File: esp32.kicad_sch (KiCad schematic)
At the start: 20 parts, among them SW4 PTS526_SM08_SMTR2_LFS

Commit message: more routing
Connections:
- net RFM95W_DI0: now reaches IC?.18 (IO14)
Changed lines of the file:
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@@
+    )
+  )
+  (global_label "RFM95W_DI0" (shape input) (at 111.76 54.61 180) (fields_autoplaced)
+    (effects (font (size 1.27 1.27)) (justify right))
+    (property "Intersheetrefs" "${INTERSHEET_REFS}" (at 97.0425 54.61 0)
+      (effects (font (size 1.27 1.27)) (justify right) hide)
     )
   )

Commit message: more routing
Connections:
- net VBUS: now also J?.A4 (VBUS), J?.A9 (VBUS), J?.B4 (VBUS), J?.B9 (VBUS)
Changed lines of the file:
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@@
+    )
+  )
+  (global_label "VBUS" (shape input) (at 265.43 118.11 0) (fields_autoplaced)
+    (effects (font (size 1.27 1.27)) (justify left))
+    (property "Intersheetrefs" "${INTERSHEET_REFS}" (at 273.3138 118.11 0)
+      (effects (font (size 1.27 1.27)) (justify left) hide)
     )
   )

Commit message: significant amount of routing done
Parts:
- removed SW4: PTS526_SM08_SMTR2_LFS, PTS526_SM08_SMTR2_LFS:SW_PTS526_SM08_SMTR2_LFS, symbol PTS526_SM08_SMTR2_LFS:PTS526_SM08_SMTR2_LFS
- removed SW?: TDD01H0SB1R, TDD01H0SB1R:SOT175P420X230-3N, symbol TDD01H0SB1R:TDD01H0SB1R
- added D? (x8): LED, LED_SMD:LED_0402_1005Metric, symbol Device:LED
- added R? (x8): 2.2k, Resistor_SMD:R_0402_1005Metric, symbol Device:R
- added S1: CJS-1200TA, CJS-1200TA:SW_CJS-1200TA, symbol CJS-1200TA:CJS-1200TA
- added S3: B3U-1000P, B3U-1000P:SW_B3U-1000P, symbol B3U-1000P:B3U-1000P
- D?: value WS2812B -> WS2812B-2020; footprint LED_SMD:LED_WS2812B_PLCC4_5.0x5.0mm_P3.2mm -> LED_SMD:LED_WS2812B-2020_PLCC4_2.0x2.0mm
- R? (x3): footprint Resistor_SMD:R_0603_1608Metric -> Resistor_SMD:R_0402_1005Metric
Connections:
- net ESP32-EN: now also S3.2
- net ESP32-GPIO0: now also S1.3
- net ESP32-RX0: no longer IC?.40 (RXD0)
- net ESP32-TX0: no longer IC?.39 (TXD0)
- net GND: now also D?.1 (K), D?.1 (K), D?.1 (K), D?.1 (K), D?.1 (K), D?.1 (K), D?.1 (K), D?.1 (K), S1.2, S3.1
- net RFM95W_RST: now reaches IC?.13 (IO9)
- net CROSS_UART: now reaches IC?.34 (IO38)
- net CROSS_UART: now also R?.2
- net CROSS_I2C: now reaches IC?.35 (IO39)
- net CROSS_I2C: now also R?.2
- net CROSS_SPI: now reaches IC?.36 (IO40)
- net CROSS_SPI: now also R?.2
- net RFD_900: now reaches IC?.37 (IO41)
- net RFD_900: now also R?.2
- net SPI-1_ESP32: now reaches IC?.38 (IO42)
- net SPI-1_ESP32: now also R?.2
- net I2C-1_STM32: now reaches IC?.41 (IO45)
- net I2C-1_STM32: now also R?.2
- net BUZZ_IN: now reaches IC?.5 (IO1)
- new net: D?.2 (A), R?.1 (x8)
- new net SPI-1_STM32: IC?.39 (TXD0), R?.2
- new net SPI-2_STM32: IC?.40 (RXD0), R?.2
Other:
- moved on the sheet: C?, R17

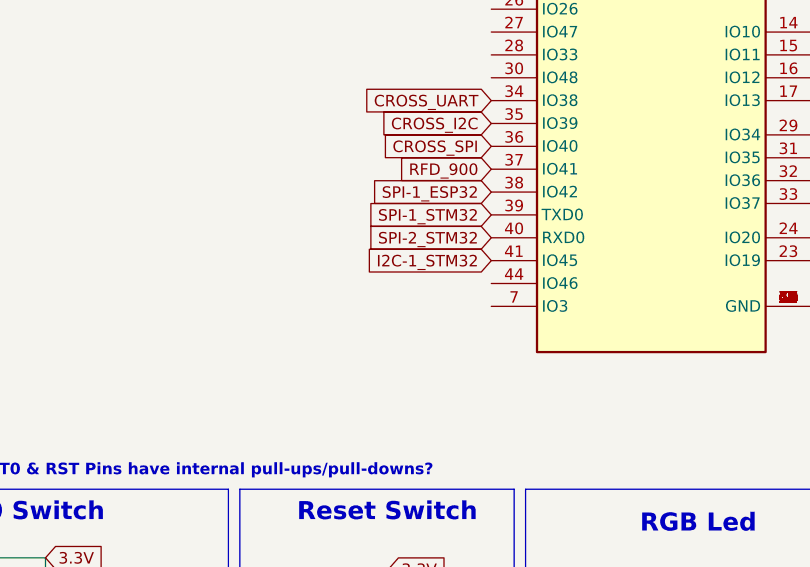
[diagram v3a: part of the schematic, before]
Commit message: signals routed
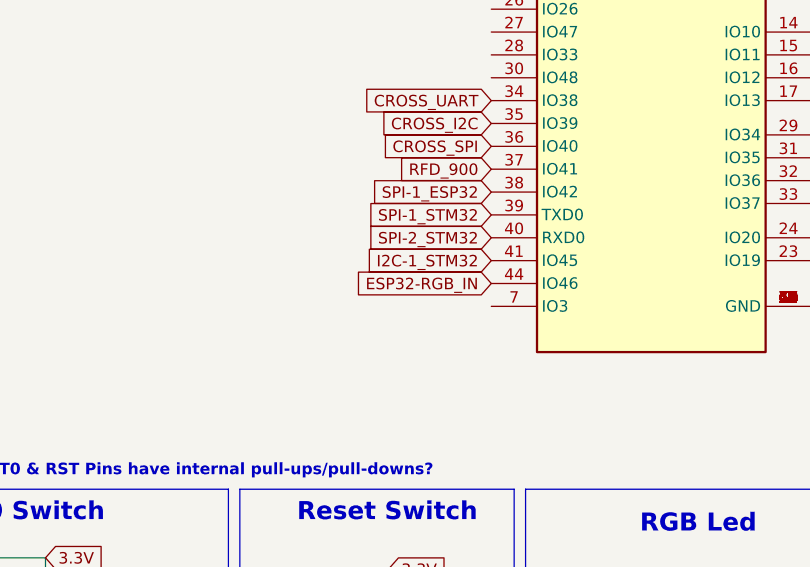
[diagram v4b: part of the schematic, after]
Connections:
- net ESP32-RGB_IN: now also IC?.44 (IO46)
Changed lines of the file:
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@@
+    )
+  )
+  (global_label "ESP32-RGB_IN" (shape input) (at 111.76 90.17 180) (fields_autoplaced)
+    (effects (font (size 1.27 1.27)) (justify right))
+    (property "Intersheetrefs" "${INTERSHEET_REFS}" (at 94.442 90.17 0)
+      (effects (font (size 1.27 1.27)) (justify right) hide)
     )
   )

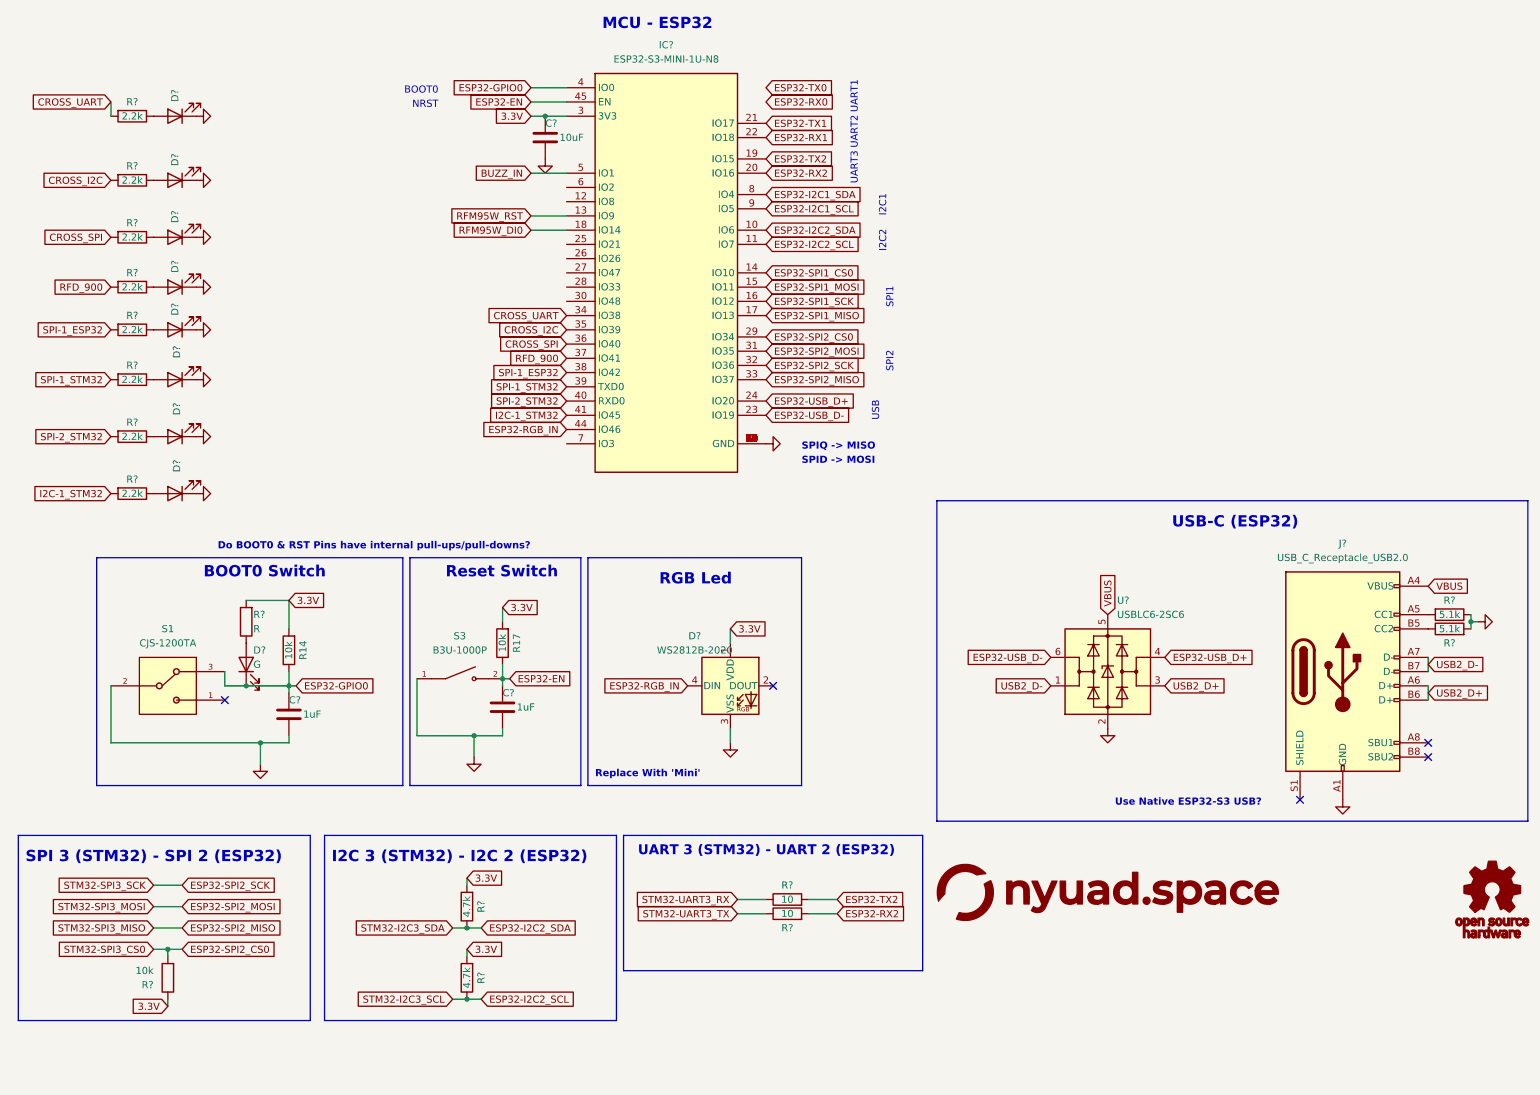
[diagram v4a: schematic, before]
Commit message: updated schematics
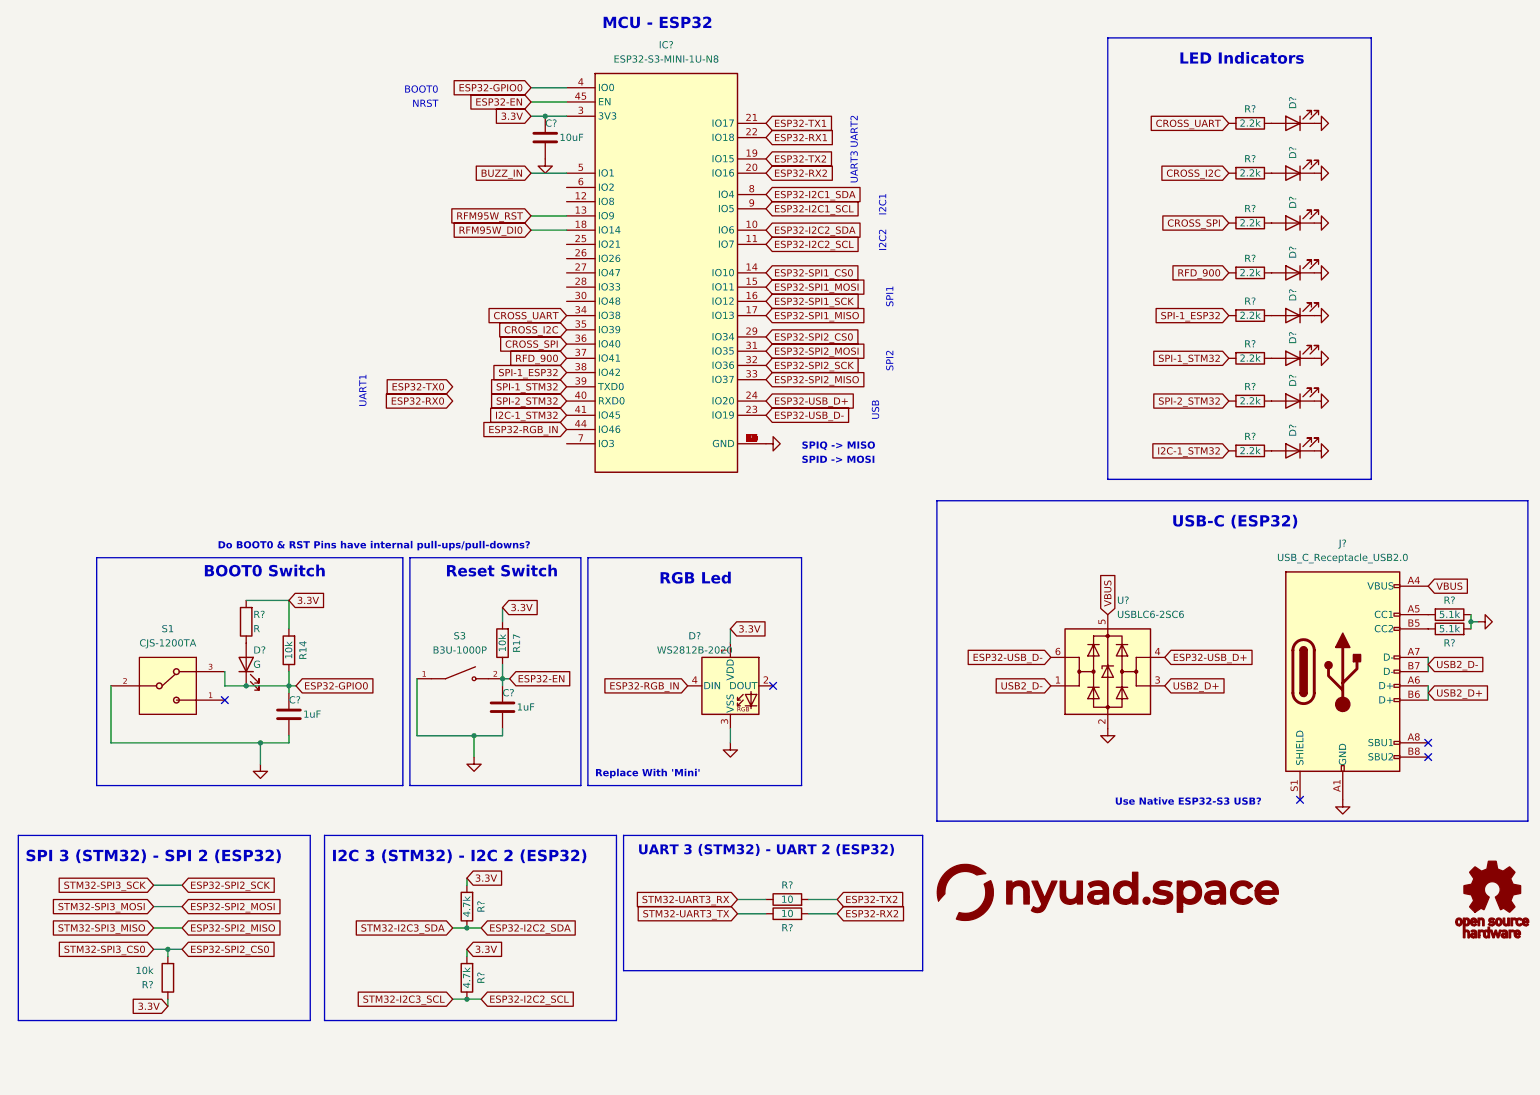
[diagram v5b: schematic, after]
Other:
- note added: "LED Indicators"
- moved on the sheet: D?, R?

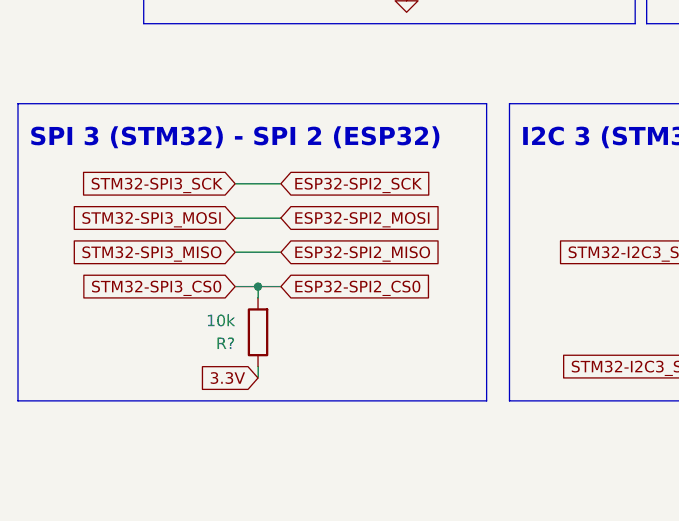
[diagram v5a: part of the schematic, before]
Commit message: added power planes
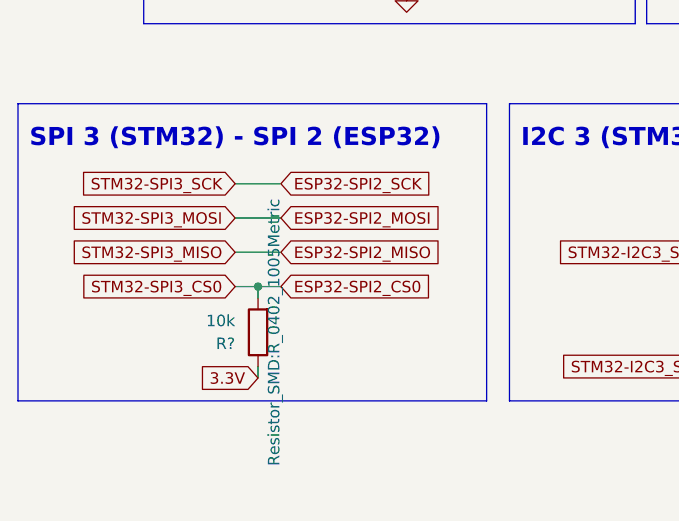
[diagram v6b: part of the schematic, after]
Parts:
- R? (x3): footprint Resistor_SMD:R_0402_1005Metric -> Resistor_SMD:R_0603_1608Metric
- R?: footprint Resistor_SMD:R_0603_1608Metric -> Resistor_SMD:R_0402_1005Metric
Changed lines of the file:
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@@
       (effects (font (size 1.27 1.27)) (justify right))
     )
-    (property "Footprint" "Resistor_SMD:R_0402_1005Metric" (at 56.388 124.46 90)
+    (property "Footprint" "Resistor_SMD:R_0603_1608Metric" (at 56.388 124.46 90)
       (effects (font (size 1.27 1.27)) hide)
     )
@@
       (effects (font (size 1.27 1.27)))
     )
-    (property "Footprint" "Resistor_SMD:R_0402_1005Metric" (at 269.24 121.412 90)
+    (property "Footprint" "Resistor_SMD:R_0603_1608Metric" (at 269.24 121.412 90)
       (effects (font (size 1.27 1.27)) hide)
     )
@@
       (effects (font (size 1.27 1.27)) (justify left))
     )
-    (property "Footprint" "Resistor_SMD:R_0603_1608Metric" (at 42.418 187.96 90)
-      (effects (font (size 1.27 1.27)) hide)
+    (property "Footprint" "Resistor_SMD:R_0402_1005Metric" (at 42.418 187.96 90)
+      (effects (font (size 1.27 1.27)))
     )
     (property "Datasheet" "~" (at 40.64 187.96 0)
@@
       (effects (font (size 1.27 1.27)))
     )
-    (property "Footprint" "Resistor_SMD:R_0402_1005Metric" (at 269.24 127.508 90)
-      (effects (font (size 1.27 1.27)) hide)
-    )
+    (property "Footprint" "Resistor_SMD:R_0603_1608Metric" (at 269.24 127.508 90)
+      (effects (font (size 1.27 1.27)) hide)
+    )
